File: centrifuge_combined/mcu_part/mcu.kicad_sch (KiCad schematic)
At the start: 22 parts

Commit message: Board appears ok
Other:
- title: (none) -> VGA Centrifuge
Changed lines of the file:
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@@
 (kicad_sch (version 20211123) (generator eeschema)
   (paper "A4")
+  (title_block
+    (title "VGA Centrifuge")
+    (date "2022-10-03")
+    (rev "R2")
+  )
   (junction (at 144.145 176.53) (diameter 0) (color 0 0 0 0)
   )

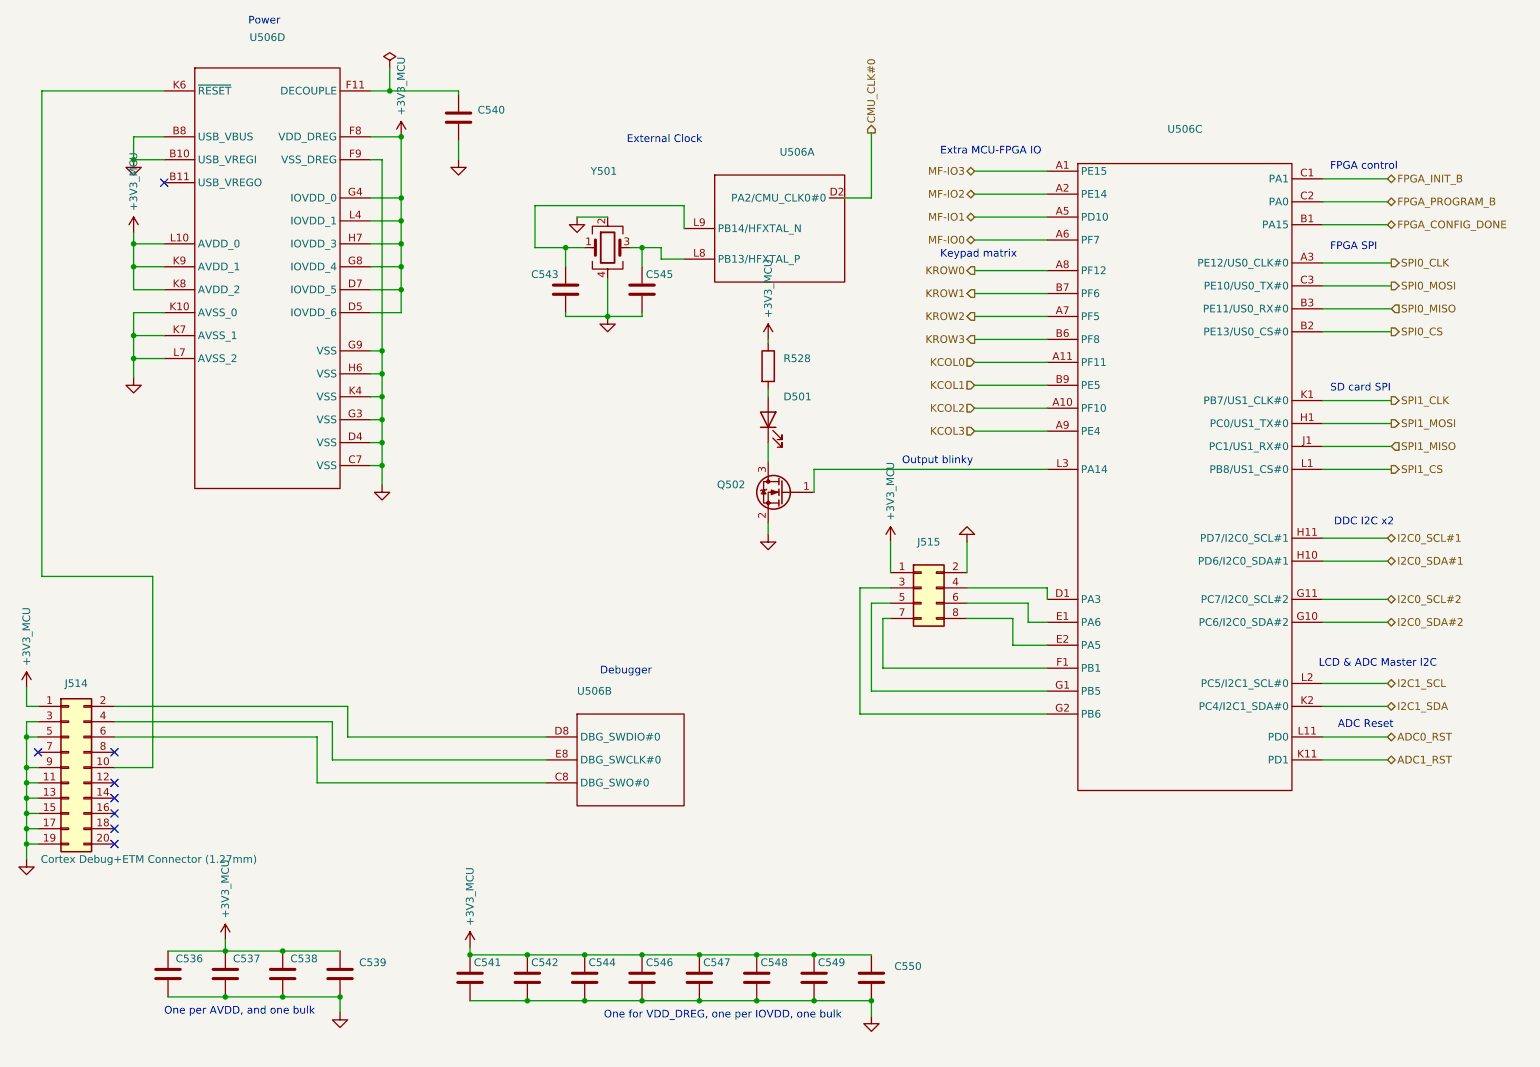
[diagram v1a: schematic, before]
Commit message: fixed keypad hole sizes, and submitted
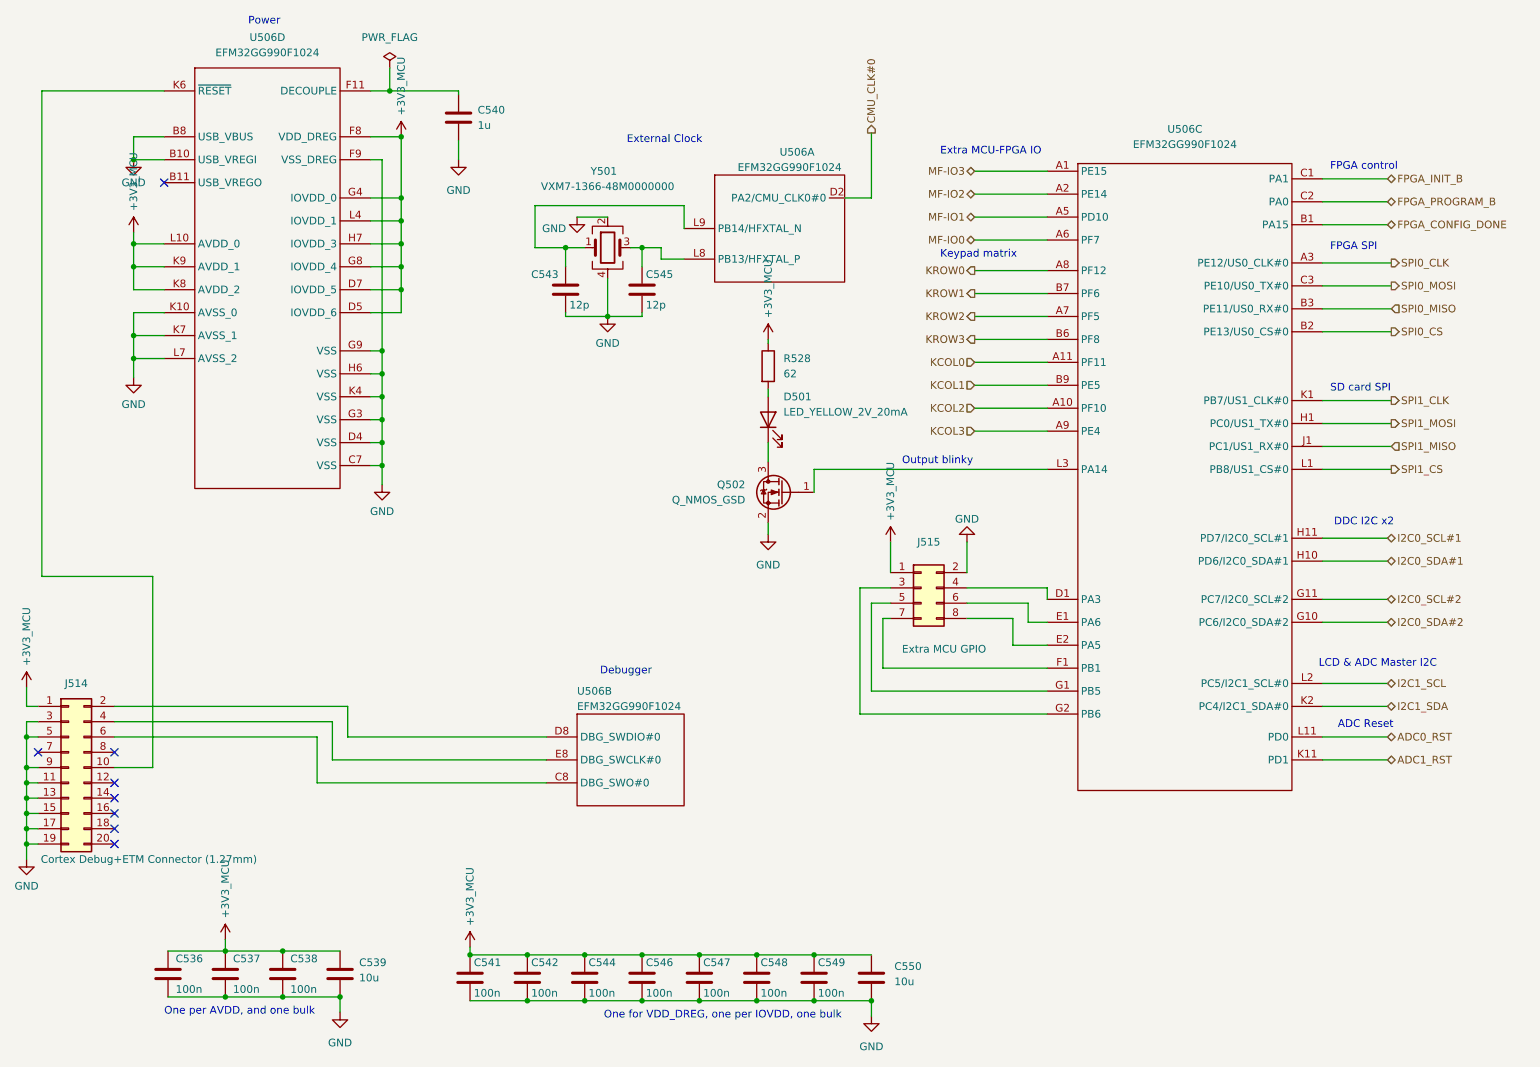
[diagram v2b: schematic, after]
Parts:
- C536, C537, C538, C541, C542, C544, C546, C547, C548, C549: value (none) -> 100n
- C539, C550: value (none) -> 10u
- C540: value (none) -> 1u
- C543, C545: value (none) -> 12p
- D501: value (none) -> LED_YELLOW_2V_20mA
- J514: value (none) -> DEBUG
- J515: value (none) -> Extra MCU GPIO
- Q502: value (none) -> Q_NMOS_GSD
- R528: value (none) -> 62
- U506: value (none) -> EFM32GG990F1024
- Y501: value (none) -> VXM7-1366-48M0000000
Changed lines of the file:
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@@
       (effects (font (size 1.27 1.27)) (justify left))
     )
-    (property "Value" "" (id 1) (at 114.3 135.255 0)
+    (property "Value" "EFM32GG990F1024" (id 1) (at 114.3 135.255 0)
       (effects (font (size 1.27 1.27)) (justify left))
     )
@@
       (effects (font (size 1.27 1.27)) hide)
     )
-    (property "Value" "" (id 1) (at 22.86 165.1 0))
+    (property "Value" "GND" (id 1) (at 22.86 165.1 0))
     (property "Footprint" "" (id 2) (at 22.86 160.655 0)
       (effects (font (size 1.27 1.27)) hide)
@@
       (effects (font (size 1.27 1.27)) hide)
     )
-    (property "Value" "" (id 1) (at 163.195 191.77 0))
+    (property "Value" "GND" (id 1) (at 163.195 191.77 0))
     (property "Footprint" "" (id 2) (at 163.195 186.69 0)
       (effects (font (size 1.27 1.27)) hide)
@@
       (effects (font (size 1.27 1.27)) (justify left))
     )
-    (property "Value" "" (id 1) (at 154.305 182.88 0)
+    (property "Value" "100n" (id 1) (at 154.305 182.88 0)
       (effects (font (size 1.27 1.27)) (justify left))
     )
@@
       (effects (font (size 1.27 1.27)) hide)
     )
-    (property "Value" "" (id 1) (at 179.07 104.14 0))
+    (property "Value" "GND" (id 1) (at 179.07 104.14 0))
     (property "Footprint" "" (id 2) (at 179.07 107.95 0)
       (effects (font (size 1.27 1.27)) hide)
@@
     (in_bom yes) (on_board yes)
     (property "Reference" "Y501" (id 0) (at 118.745 46.355 0))
-    (property "Value" "" (id 1) (at 119.38 48.895 0))
+    (property "Value" "VXM7-1366-48M0000000" (id 1) (at 119.38 48.895 0))
     (property "Footprint" "" (id 2) (at 119.38 59.055 0)
       (effects (font (size 1.27 1.27)) hide)
@@
       (effects (font (size 1.27 1.27)) (justify left))
     )
-    (property "Value" "" (id 1) (at 167.005 180.9749 0)
+    (property "Value" "10u" (id 1) (at 167.005 180.9749 0)
       (effects (font (size 1.27 1.27)) (justify left))
     )
@@
       (effects (font (size 1.27 1.27)) hide)
     )
-    (property "Value" "" (id 1) (at 40.64 85.09 0))
+    (property "Value" "GND" (id 1) (at 40.64 85.09 0))
     (property "Footprint" "" (id 2) (at 40.64 80.645 0)
       (effects (font (size 1.27 1.27)) hide)
@@
       (effects (font (size 1.27 1.27)) (justify left))
     )
-    (property "Value" "" (id 1) (at 116.205 182.88 0)
+    (property "Value" "100n" (id 1) (at 116.205 182.88 0)
       (effects (font (size 1.27 1.27)) (justify left))
     )
@@
     (in_bom yes) (on_board yes)
     (property "Reference" "J514" (id 0) (at 31.115 131.445 0))
-    (property "Value" "" (id 1) (at 31.115 130.81 0)
+    (property "Value" "DEBUG" (id 1) (at 31.115 130.81 0)
       (effects (font (size 1.27 1.27)) hide)
     )
@@
       (effects (font (size 1.27 1.27)) (justify left))
     )
-    (property "Value" "" (id 1) (at 97.155 182.88 0)
+    (property "Value" "100n" (id 1) (at 97.155 182.88 0)
       (effects (font (size 1.27 1.27)) (justify left))
     )
@@
       (effects (font (size 1.27 1.27)) hide)
     )
-    (property "Value" "" (id 1) (at 74.93 191.135 0))
+    (property "Value" "GND" (id 1) (at 74.93 191.135 0))
     (property "Footprint" "" (id 2) (at 74.93 186.055 0)
       (effects (font (size 1.27 1.27)) hide)
@@
       (effects (font (size 1.27 1.27)) hide)
     )
-    (property "Value" "" (id 1) (at 94.615 49.53 0))
+    (property "Value" "GND" (id 1) (at 94.615 49.53 0))
     (property "Footprint" "" (id 2) (at 94.615 44.45 0)
       (effects (font (size 1.27 1.27)) hide)
@@
       (effects (font (size 1.27 1.27)) (justify left))
     )
-    (property "Value" "" (id 1) (at 66.675 182.245 0)
+    (property "Value" "100n" (id 1) (at 66.675 182.245 0)
       (effects (font (size 1.27 1.27)) (justify left))
     )
@@
       (effects (font (size 1.27 1.27)) hide)
     )
-    (property "Value" "" (id 1) (at 83.185 24.13 0))
+    (property "Value" "PWR_FLAG" (id 1) (at 83.185 24.13 0))
     (property "Footprint" "" (id 2) (at 83.185 29.21 0)
       (effects (font (size 1.27 1.27)) hide)
@@
       (effects (font (size 1.27 1.27)) hide)
     )
-    (property "Value" "" (id 1) (at 40.64 48.26 0))
+    (property "Value" "GND" (id 1) (at 40.64 48.26 0))
     (property "Footprint" "" (id 2) (at 40.64 44.45 0)
       (effects (font (size 1.27 1.27)) hide)
@@
       (effects (font (size 1.27 1.27)) (justify left))
     )
-    (property "Value" "" (id 1) (at 125.73 182.88 0)
+    (property "Value" "100n" (id 1) (at 125.73 182.88 0)
       (effects (font (size 1.27 1.27)) (justify left))
     )
@@
       (effects (font (size 1.27 1.27)) (justify left))
     )
-    (property "Value" "" (id 1) (at 140.97 45.72 0)
+    (property "Value" "EFM32GG990F1024" (id 1) (at 140.97 45.72 0)
       (effects (font (size 1.27 1.27)) (justify left))
     )
@@
       (effects (font (size 1.27 1.27)) hide)
     )
-    (property "Value" "" (id 1) (at 119.38 74.93 0))
+    (property "Value" "GND" (id 1) (at 119.38 74.93 0))
     (property "Footprint" "" (id 2) (at 119.38 70.485 0)
       (effects (font (size 1.27 1.27)) hide)
@@
       (effects (font (size 1.27 1.27)) (justify left))
     )
-    (property "Value" "" (id 1) (at 57.15 182.245 0)
+    (property "Value" "100n" (id 1) (at 57.15 182.245 0)
       (effects (font (size 1.27 1.27)) (justify left))
     )
@@
     (in_bom yes) (on_board yes)
     (property "Reference" "J515" (id 0) (at 172.72 107.95 0))
-    (property "Value" "" (id 1) (at 175.26 125.73 0))
+    (property "Value" "Extra MCU GPIO" (id 1) (at 175.26 125.73 0))
     (property "Footprint" "" (id 2) (at 171.45 115.57 0)
       (effects (font (size 1.27 1.27)) hide)
@@
       (effects (font (size 1.27 1.27)) (justify left))
     )
-    (property "Value" "" (id 1) (at 106.68 182.88 0)
+    (property "Value" "100n" (id 1) (at 106.68 182.88 0)
       (effects (font (size 1.27 1.27)) (justify left))
     )
@@
       (effects (font (size 1.27 1.27)) hide)
     )
-    (property "Value" "" (id 1) (at 81.915 102.87 0))
+    (property "Value" "GND" (id 1) (at 81.915 102.87 0))
     (property "Footprint" "" (id 2) (at 81.915 98.425 0)
       (effects (font (size 1.27 1.27)) hide)
@@
       (effects (font (size 1.27 1.27)) (justify left))
     )
-    (property "Value" "" (id 1) (at 78.105 180.3399 0)
+    (property "Value" "10u" (id 1) (at 78.105 180.3399 0)
       (effects (font (size 1.27 1.27)) (justify left))
     )
@@
       (effects (font (size 1.27 1.27)) (justify left))
     )
-    (property "Value" "" (id 1) (at 135.255 182.88 0)
+    (property "Value" "100n" (id 1) (at 135.255 182.88 0)
       (effects (font (size 1.27 1.27)) (justify left))
     )
@@
     (in_bom yes) (on_board yes) (fields_autoplaced)
     (property "Reference" "U506" (id 0) (at 62.865 24.13 0))
-    (property "Value" "" (id 1) (at 62.865 26.67 0))
+    (property "Value" "EFM32GG990F1024" (id 1) (at 62.865 26.67 0))
     (property "Footprint" "" (id 2) (at 63.5 15.24 0)
       (effects (font (size 1.27 1.27)) hide)
@@
       (effects (font (size 1.27 1.27)) hide)
     )
-    (property "Value" "" (id 1) (at 146.05 111.76 0))
+    (property "Value" "GND" (id 1) (at 146.05 111.76 0))
     (property "Footprint" "" (id 2) (at 146.05 106.68 0)
       (effects (font (size 1.27 1.27)) hide)
@@
     (in_bom yes) (on_board yes) (fields_autoplaced)
     (property "Reference" "U506" (id 0) (at 215.265 39.37 0))
-    (property "Value" "" (id 1) (at 215.265 41.91 0))
+    (property "Value" "EFM32GG990F1024" (id 1) (at 215.265 41.91 0))
     (property "Footprint" "" (id 2) (at 213.995 46.355 0)
       (effects (font (size 1.27 1.27)) hide)
@@
       (effects (font (size 1.27 1.27)) (justify left))
     )
-    (property "Value" "" (id 1) (at 125.73 68.58 0)
+    (property "Value" "12p" (id 1) (at 125.73 68.58 0)
       (effects (font (size 1.27 1.27)) (justify left))
     )
@@
       (effects (font (size 1.27 1.27)) (justify left))
     )
-    (property "Value" "" (id 1) (at 144.78 182.88 0)
+    (property "Value" "100n" (id 1) (at 144.78 182.88 0)
       (effects (font (size 1.27 1.27)) (justify left))
     )
@@
       (effects (font (size 1.27 1.27)) (justify left))
     )
-    (property "Value" "" (id 1) (at 47.625 182.245 0)
+    (property "Value" "100n" (id 1) (at 47.625 182.245 0)
       (effects (font (size 1.27 1.27)) (justify left))
     )
@@
       (effects (font (size 1.27 1.27)) (justify right))
     )
-    (property "Value" "" (id 1) (at 148.59 86.36 90)
+    (property "Value" "LED_YELLOW_2V_20mA" (id 1) (at 148.59 86.36 90)
       (effects (font (size 1.27 1.27)) (justify right))
     )
@@
       (effects (font (size 1.27 1.27)) (justify left))
     )
-    (property "Value" "" (id 1) (at 113.03 68.58 0)
+    (property "Value" "12p" (id 1) (at 113.03 68.58 0)
       (effects (font (size 1.27 1.27)) (justify left))
     )
@@
       (effects (font (size 1.27 1.27)) (justify left))
     )
-    (property "Value" "" (id 1) (at 148.59 80.0099 0)
+    (property "Value" "62" (id 1) (at 148.59 80.0099 0)
       (effects (font (size 1.27 1.27)) (justify left))
     )
@@
       (effects (font (size 1.27 1.27)) hide)
     )
-    (property "Value" "" (id 1) (at 110.49 55.88 0))
+    (property "Value" "GND" (id 1) (at 110.49 55.88 0))
     (property "Footprint" "" (id 2) (at 114.3 53.975 0)
       (effects (font (size 1.27 1.27)) hide)
@@
       (effects (font (size 1.27 1.27)) (justify right))
     )
-    (property "Value" "" (id 1) (at 97.79 38.7349 0)
+    (property "Value" "1u" (id 1) (at 97.79 38.7349 0)
       (effects (font (size 1.27 1.27)) (justify right))
     )
@@
       (effects (font (size 1.27 1.27)) (justify left))
     )
-    (property "Value" "" (id 1) (at 142.24 100.9649 0)
-      (effects (font (size 1.27 1.27)) (justify left))
-    )
+    (property "Value" "Q_NMOS_GSD" (id 1) (at 142.24 100.9649 0)
+      (effects (font (size 1.27 1.27)) (justify left))
+    )
